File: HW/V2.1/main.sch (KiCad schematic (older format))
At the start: 28 parts, among them IC1 RT9466, J4 USB-C, T1 TS-1136EVW

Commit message: updated values
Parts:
- C23: value 4.7u 25V -> 10u 25V
- NTC1: value 10k -> DNP
- T1: value TS-1136EVW -> Panasonic_EVQPUL_EVQPUC
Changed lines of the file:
@@
 P 7350 4150
 F 0 "NTC1" H 7420 4203 60  0000 L CNN
-F 1 "10k" H 7420 4097 60  0000 L CNN
+F 1 "DNP" H 7420 4097 60  0000 L CNN
 F 2 "Resistor_SMD:R_0603_1608Metric" H 7350 4010 60  0001 C CNN
 F 3 "" H 7350 4010 60  0000 C CNN
@@
 P 6150 4650
 F 0 "T1" H 5940 4850 60  0000 L BNN
-F 1 "TS-1136EVW" H 5940 4350 60  0000 L BNN
+F 1 "Panasonic_EVQPUL_EVQPUC" H 5940 4350 60  0000 L BNN
 F 2 "Button_Switch_SMD:Panasonic_EVQPUL_EVQPUC" H 5940 4350 60  0001 C CNN
 F 3 "" H 5940 4350 60  0000 C CNN
@@
 P 2250 3350
 F 0 "C23" V 2260 3160 60  0000 R TNN
-F 1 "4.7u 25V" V 2160 3160 60  0000 R TNN
+F 1 "10u 25V" V 2160 3160 60  0000 R TNN
 F 2 "Capacitor_SMD:C_0805_2012Metric" H 2160 3160 60  0001 C CNN
 F 3 "" H 2160 3160 60  0000 C CNN

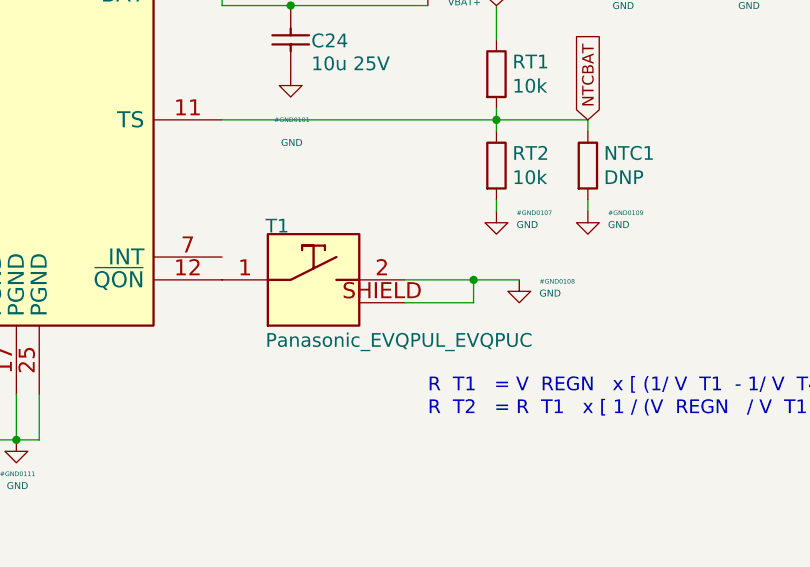
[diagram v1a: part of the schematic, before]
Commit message: added touch ic, fixed sk6812
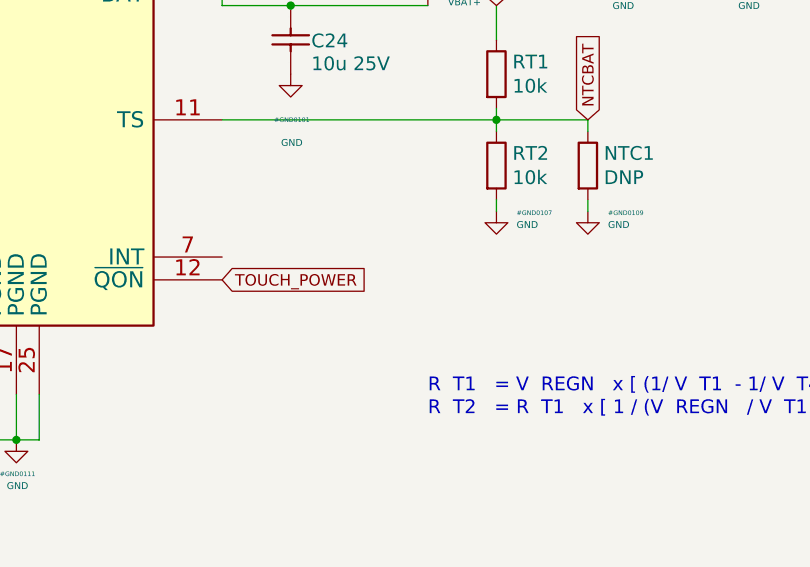
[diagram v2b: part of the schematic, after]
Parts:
- removed T1: Panasonic_EVQPUL_EVQPUC, Button_Switch_SMD:Panasonic_EVQPUL_EVQPUC, symbol EO:TS-1136EVW
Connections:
- net TOUCH_POWER: now reaches IC1.12 (~QON)
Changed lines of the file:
@@
 REGN
-$Comp
-L power:GND #GND0108
-U 1 1 5D2B582D
-P 7050 4650
-F 0 "#GND0108" H 7138 4643 20  0000 L CNN
-F 1 "GND" H 7138 4591 30  0000 L CNN
-F 2 "" H 7050 4650 70  0000 C CNN
-F 3 "" H 7050 4650 70  0000 C CNN
-	1    7050 4650
-	1    0    0    -1
-$EndComp
 $Comp
 L power:GND #GND0109
@@
 Wire Wire Line
 	5950 8400 5950 8800
-Wire Wire Line
-	6850 4650 7050 4650
-Wire Wire Line
-	6550 4650 6850 4650
-Wire Wire Line
-	6850 4750 6550 4750
-Wire Wire Line
-	6850 4650 6850 4750
 Wire Wire Line
 	5750 2900 5850 2900
@@
 Connection ~ 6050 3150
 Connection ~ 6050 2950
-Connection ~ 6850 4650
 Connection ~ 7250 2950
 Connection ~ 8050 2950
@@
 	1    5650 9400
 	0    -1   -1   0
-$EndComp
-$Comp
-L EO:TS-1136EVW T1
-U 1 1 5D2B5811
-P 6150 4650
-F 0 "T1" H 5940 4850 60  0000 L BNN
-F 1 "Panasonic_EVQPUL_EVQPUC" H 5940 4350 60  0000 L BNN
-F 2 "Button_Switch_SMD:Panasonic_EVQPUL_EVQPUC" H 5940 4350 60  0001 C CNN
-F 3 "" H 5940 4350 60  0000 C CNN
-	1    6150 4650
-	1    0    0    -1
 $EndComp
 $Comp
@@
 $EndComp
 Connection ~ 2950 2650
+Text GLabel 5750 4650 2    50   Input ~ 0
+TOUCH_POWER
 $EndSCHEMATC

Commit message: enlarged pads
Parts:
- R29: footprint Resistor_SMD:R_0805_2012Metric -> Resistor_SMD:R_0603_1608Metric
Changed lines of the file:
@@
 F 0 "R29" V 3373 3850 60  0000 C CNN
 F 1 "698" V 3479 3850 60  0000 C CNN
-F 2 "Resistor_SMD:R_0805_2012Metric" H 3250 3610 60  0001 C CNN
+F 2 "Resistor_SMD:R_0603_1608Metric" H 3250 3610 60  0001 C CNN
 F 3 "" H 3250 3610 60  0000 C CNN
 	1    3250 3850
